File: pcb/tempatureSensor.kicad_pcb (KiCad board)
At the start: 2 copper layers, 17 parts, among them J1 Screw_Terminal_01x03, J2 Screw_Terminal_01x03, J3 Screw_Terminal_01x02, J4 Screw_Terminal_01x03, J5 Screw_Terminal_01x03, J6 Screw_Terminal_01x03, J7 Conn_01x04, K3 Relay_SPDT, K4 Relay_SPDT, K5 Relay_SPDT, U1 ESP32-C3-WROOM-02, U2 AMS1117-3.3, U3 AM2302

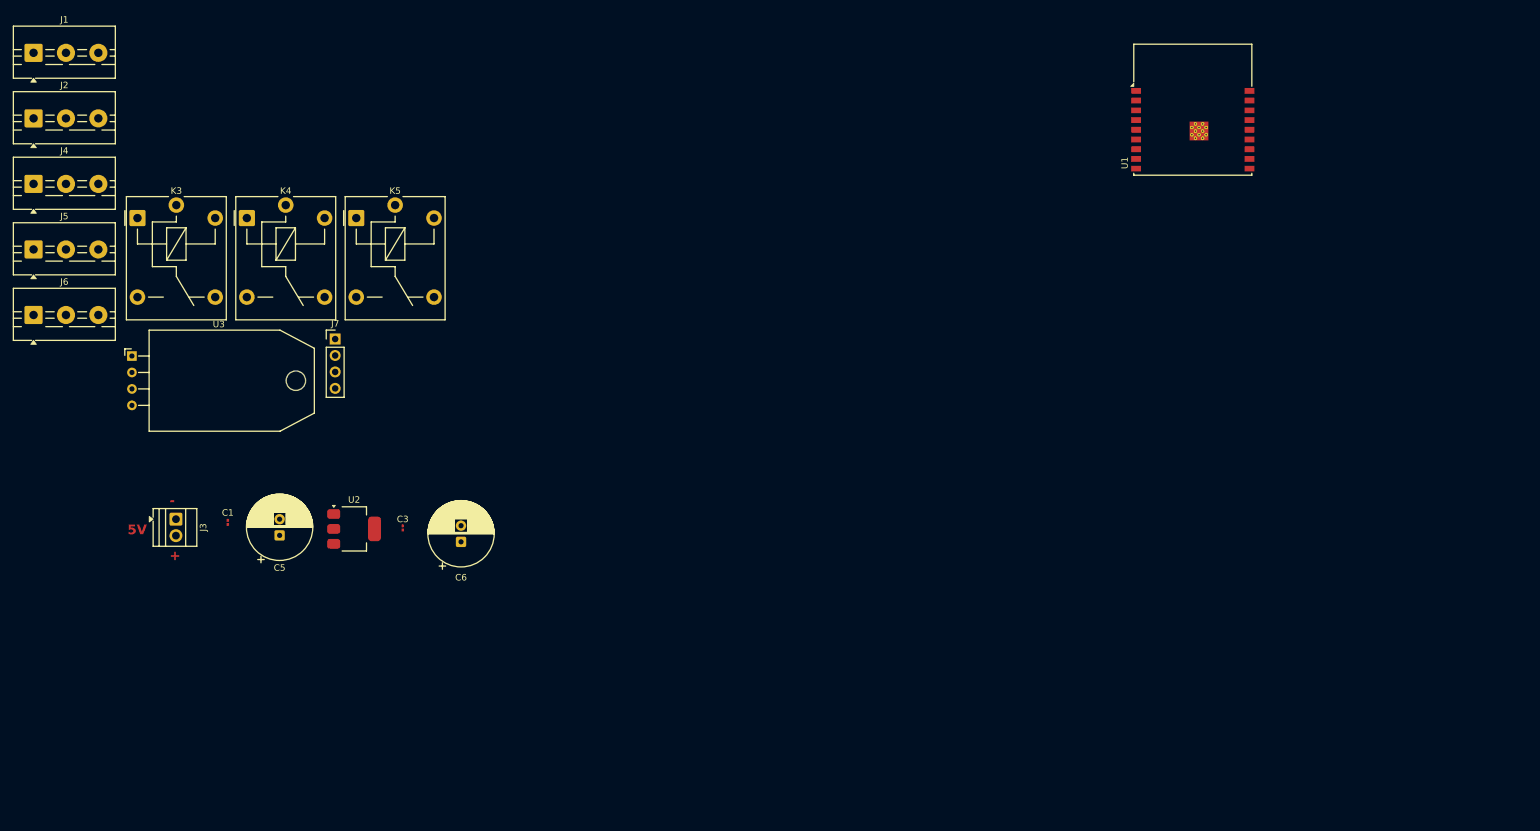
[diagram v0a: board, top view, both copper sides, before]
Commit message: aligning everithing on the pcb vol. 1
aligning the relays
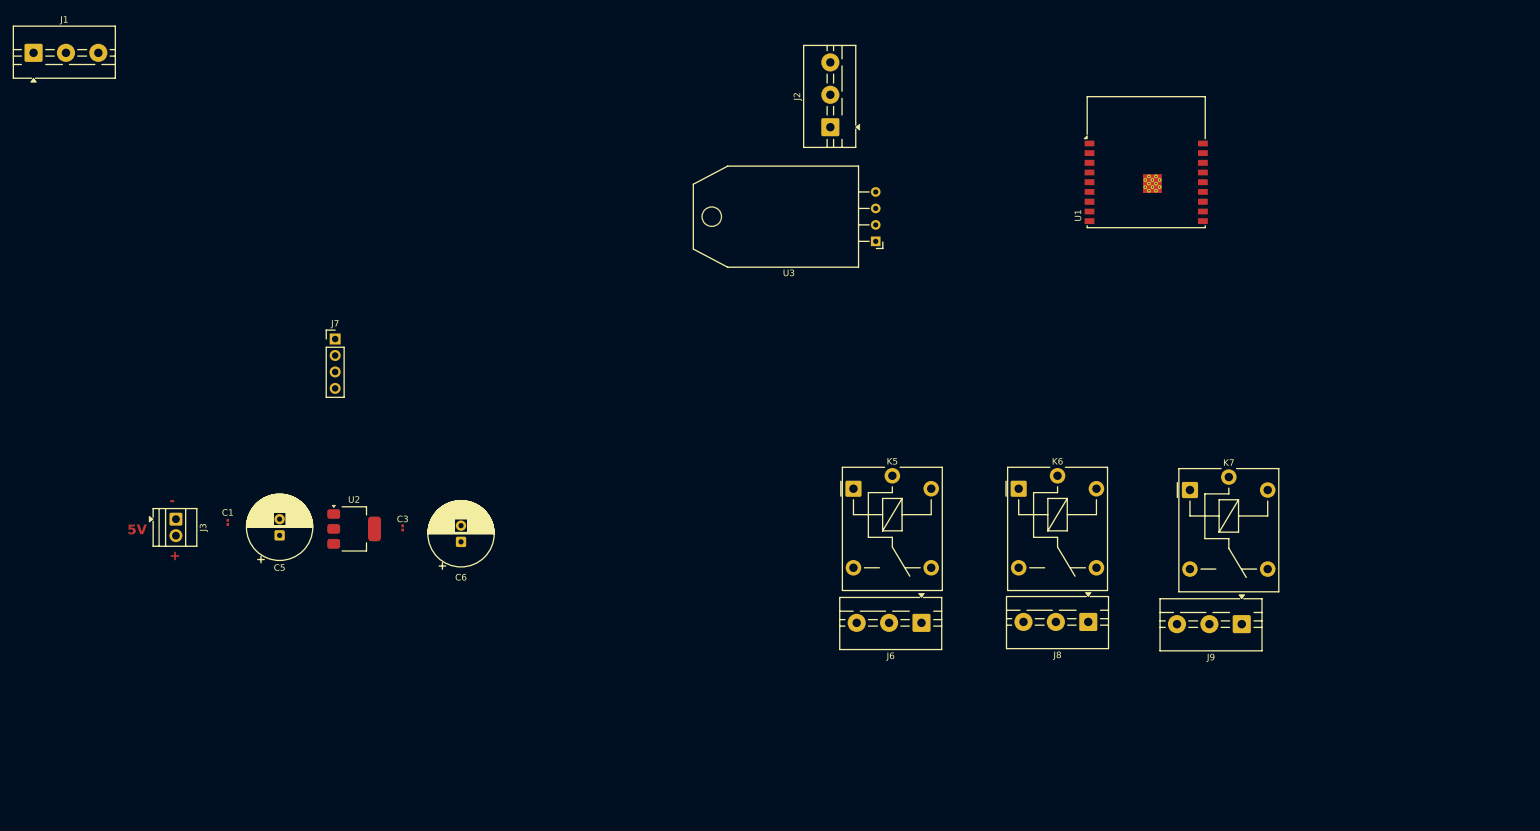
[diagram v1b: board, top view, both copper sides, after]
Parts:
- removed J4, J5: Screw_Terminal_01x03, TerminalBlock:TerminalBlock_MaiXu_MX126-5.0-03P_1x03_P5.00mm
- removed K3, K4: Relay_SPDT, Relay_THT:Relay_SPDT_Finder_36.11
- added J8: Screw_Terminal_01x03, TerminalBlock:TerminalBlock_MaiXu_MX126-5.0-03P_1x03_P5.00mm, F.Cu at (180.3, 109.9)
- added J9: Screw_Terminal_01x03, TerminalBlock:TerminalBlock_MaiXu_MX126-5.0-03P_1x03_P5.00mm, F.Cu at (204.0, 110.2)
- added K6: Relay_SPDT, Relay_THT:Relay_SPDT_Finder_36.11, F.Cu at (169.6, 89.3)
- added K7: Relay_SPDT, Relay_THT:Relay_SPDT_Finder_36.11, F.Cu at (196.0, 89.5)
- moved J6 145.0 mm to (154.6, 110.0), turned to 180 degrees
- moved J2 123.0 mm to (140.5, 33.5), turned to 90 degrees
- moved U3 116.1 mm to (147.5, 51.1), turned to 180 degrees
- moved K5 87.4 mm to (144.1, 89.3)
- moved U1 10.8 mm to (189.2, 42.0)
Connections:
- K5 pad 11: Net-(J6-Pin_3) -> Net-(J6-Pin_2)
- K5 pad 14: Net-(J6-Pin_2) -> Net-(J6-Pin_3)
- U3 pad 1: unconnected-(U3-VDD-Pad1) -> /V3.3
- U3 pad 3: Net-(U3-GND-Pad3) -> /GND
- U3 pad 4: Net-(U3-GND-Pad3) -> /GND

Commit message: aligning everithing on the pcb vol. 2
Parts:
- moved J1 134.4 mm to (140.0, 77.4), turned to 90 degrees
- moved J7 132.0 mm to (195.9, 59.4), turned to 180 degrees
- moved C1 100.2 mm to (147.6, 97.5)
- moved J3 99.9 mm to (139.3, 97.2)
- moved C5 98.8 mm to (154.3, 99.4)
- moved U2 98.7 mm to (165.6, 99.2)
- moved C3 97.1 mm to (171.5, 98.8)
- moved C6 96.1 mm to (179.6, 99.1)
- moved U3 63.1 mm to (208.0, 69.1), turned to 0 degrees
- moved J6 52.8 mm to (200.8, 135.4)
- moved K5 52.7 mm to (190.1, 114.9)
- moved K7 51.2 mm to (151.6, 114.9)
- moved J9 48.8 mm to (162.3, 135.4)
- moved J2 27.4 mm to (140.0, 60.9)
- moved K6 25.6 mm to (170.9, 114.9)
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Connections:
- J7 pad 1: unconnected-(J7-Pin_1-Pad1) -> Net-(J7-Pin_1)
- U1 pad 11: unconnected-(U1-IO20/RXD-Pad11) -> Net-(J7-Pin_1)
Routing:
- added copper zone on B.Cu, net /GND
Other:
- board outline added: 112.6 x 104.9 mm

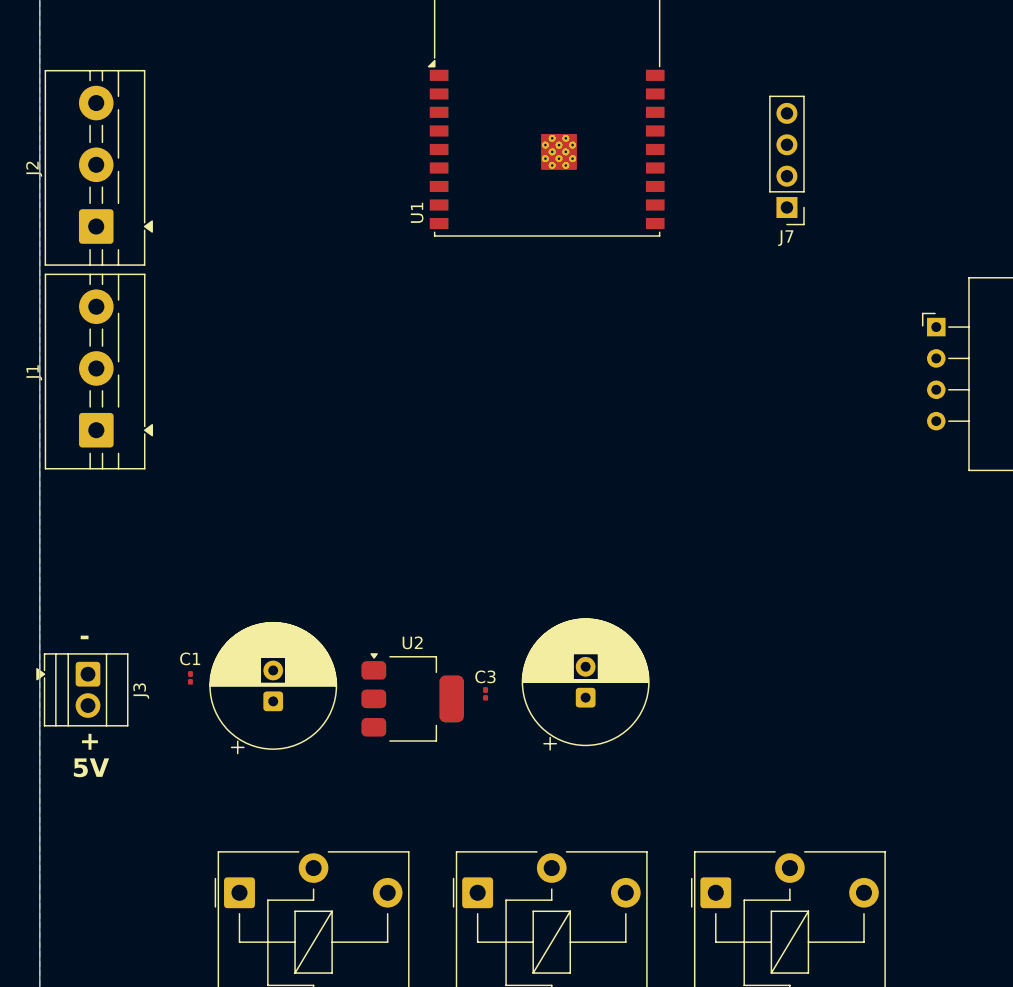
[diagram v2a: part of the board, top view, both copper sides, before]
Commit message: designing the power rails
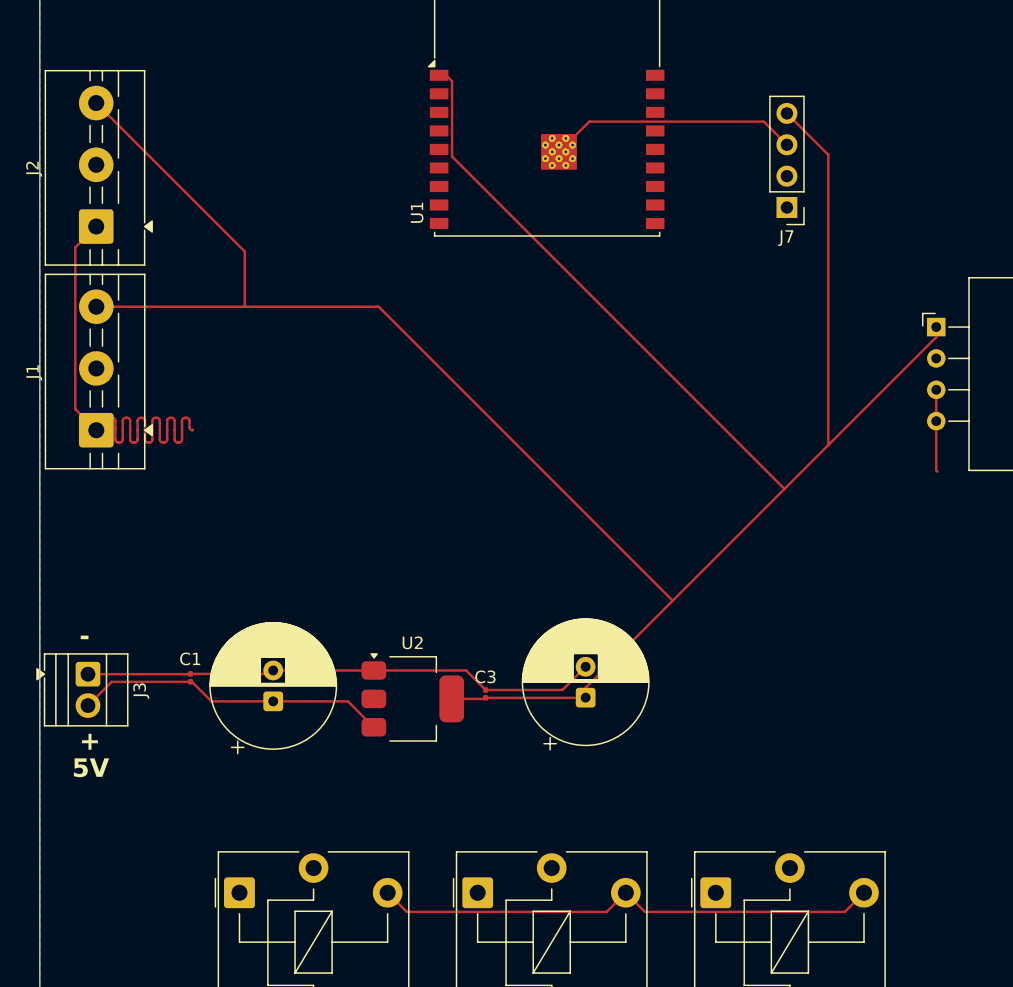
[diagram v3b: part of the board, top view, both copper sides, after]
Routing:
- net /V3.3: track 0.00 -> 204.3 mm
- net /GND: track 0.00 -> 155.0 mm
- net Net-(J3-Pin_2): track 0.00 -> 25.5 mm

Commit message: refining the conections
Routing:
- net Net-(U1-IO8): track 0.00 -> 141.8 mm
- net Net-(U1-IO7): track 0.00 -> 123.2 mm
- net /GND: track 155.0 -> 264.3 mm, vias 0 -> 4
- net Net-(U1-IO6): track 0.00 -> 106.1 mm
- net Net-(J9-Pin_2): track 0.00 -> 22.6 mm
- net Net-(J8-Pin_2): track 0.00 -> 22.6 mm
- net Net-(J6-Pin_2): track 0.00 -> 22.6 mm
- net Net-(J9-Pin_1): track 0.00 -> 8.84 mm
- net Net-(J8-Pin_1): track 0.00 -> 8.84 mm
- net Net-(J6-Pin_1): track 0.00 -> 8.84 mm
- net Net-(J9-Pin_3): track 0.00 -> 8.58 mm
- net Net-(J6-Pin_3): track 0.00 -> 8.58 mm
- net (no net): track 0.00 -> 5.76 mm

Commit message: making the grounding beter
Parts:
- moved C3 0.97 mm to (172.4, 98.4)
- moved C1 0.43 mm to (148.0, 97.6)
- moved C5 0.43 mm to (154.7, 99.5)
- moved C6 0.43 mm to (180.0, 99.2)
- moved J3 0.43 mm to (139.7, 97.3)
- moved U2 0.43 mm to (166.0, 99.3)
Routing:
- net /GND: track 264.3 -> 29.9 mm, vias 4 -> 0
- net /V3.3: track 204.3 -> 9.73 mm
- net Net-(J2-Pin_2): track 0.00 -> 29.5 mm, vias 0 -> 1
- net Net-(J1-Pin_2): track 0.00 -> 26.3 mm
- net Net-(J3-Pin_2): track 25.5 -> 0.00 mm
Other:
- board size 112.6 x 104.9 mm -> 107 x 106.7 mm

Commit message: making the power traces beter
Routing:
- net /V3.3: track 9.73 -> 198.4 mm
- net Net-(U1-IO19): track 0.00 -> 39.5 mm
- net /GND: track 29.9 -> 62.3 mm
- net Net-(J1-Pin_2): track 26.3 -> 54.4 mm, vias 0 -> 1
- net Net-(J3-Pin_2): track 0.00 -> 25.4 mm
- net Net-(J7-Pin_2): track 0.00 -> 11.0 mm, vias 0 -> 1
- net Net-(J7-Pin_1): track 0.00 -> 10.8 mm, vias 0 -> 1
- net Net-(J8-Pin_3): track 0.00 -> 8.58 mm
- net (no net): track 5.76 -> 0.00 mm

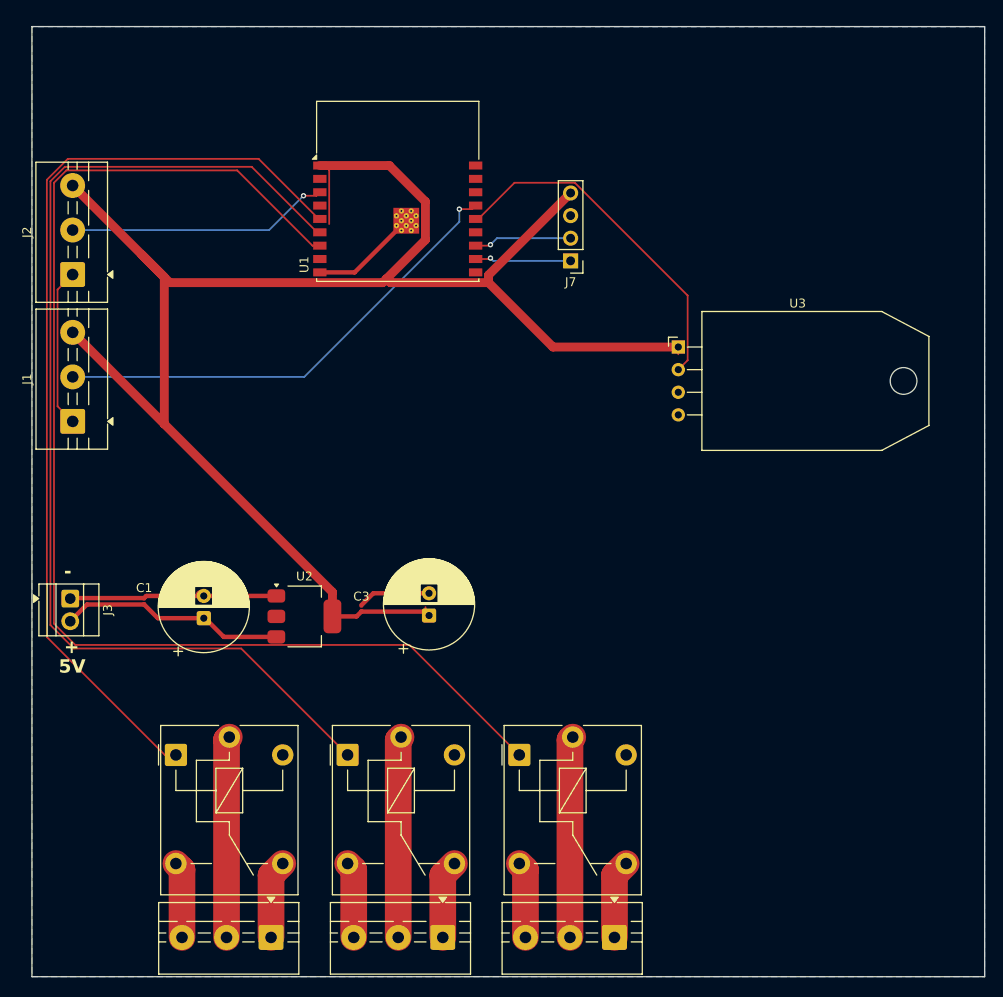
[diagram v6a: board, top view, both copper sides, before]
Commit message: adding mounthing holes
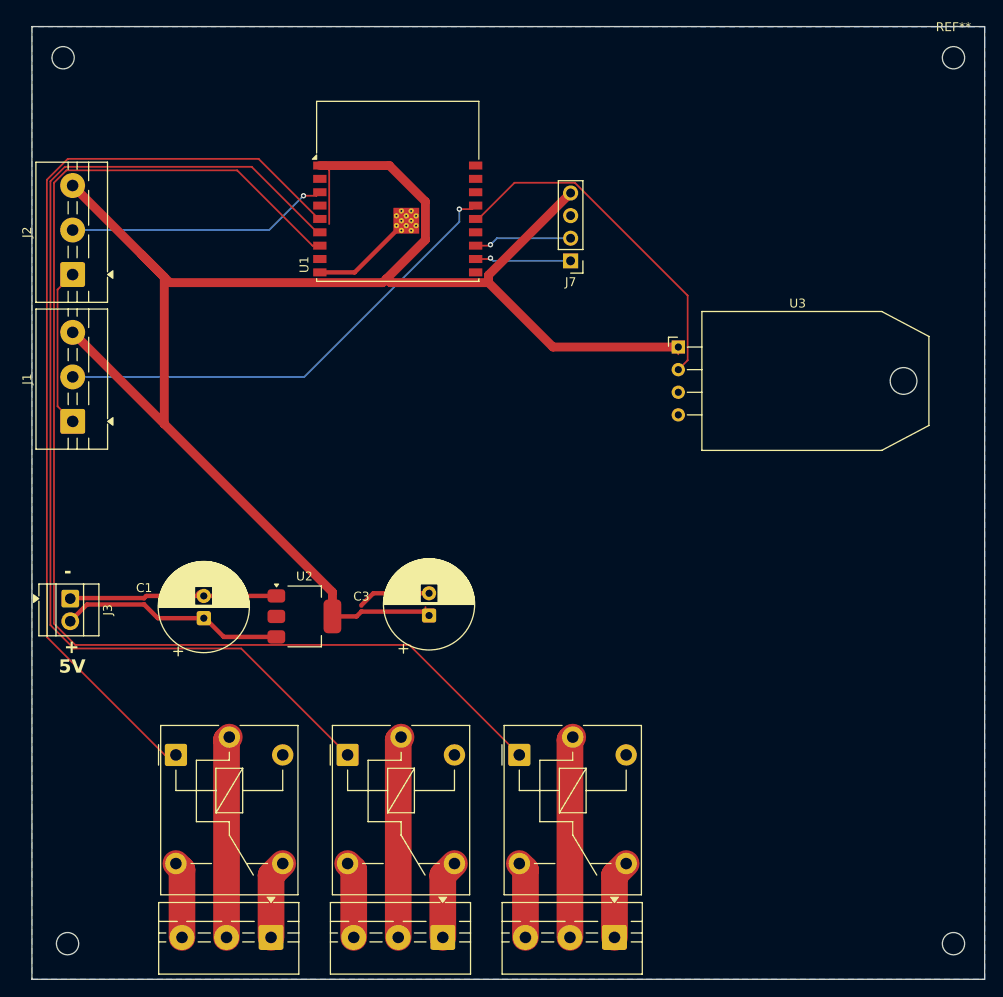
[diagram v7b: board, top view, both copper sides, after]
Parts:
- added REF**: MountingHole_2.5mm, MountingHole:MountingHole_2.5mm, F.Cu at (238.9, 136.1)
- added REF**: MountingHole_2.5mm, MountingHole:MountingHole_2.5mm, F.Cu at (139.4, 136.1)
- added REF**: MountingHole_2.5mm, MountingHole:MountingHole_2.5mm, F.Cu at (138.9, 36.6)
- added REF**: MountingHole_2.5mm, MountingHole:MountingHole_2.5mm, F.Cu at (238.9, 36.6)
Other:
- board size 107 x 106.7 mm -> 107 x 107 mm
